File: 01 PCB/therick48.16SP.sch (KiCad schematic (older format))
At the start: 172 parts, among them J1 TYPE-C-31-M12_13, J2 AVR-ISP-6_mod, K1 KEYSW, K10 KEYSW, K11 KEYSW, K12 KEYSW, K13 KEYSW, K14 KEYSW, K15 KEYSW, K16 KEYSW, K17 KEYSW, K18 KEYSW, K19 KEYSW, K2 KEYSW, K20 KEYSW, K21 KEYSW, K22 KEYSW, K23 KEYSW, K24 KEYSW, K25 KEYSW, K26 KEYSW, K27 KEYSW, K28 KEYSW, K29 KEYSW, K3 KEYSW, K30 KEYSW, K31 KEYSW, K32 KEYSW, K33 KEYSW, K34 KEYSW, K35 KEYSW, K36 KEYSW, K37 KEYSW, K38 KEYSW, K39 KEYSW, K4 KEYSW, K40 KEYSW, K41 KEYSW, K42 KEYSW, K43 KEYSW, K44 KEYSW, K45 KEYSW, K46 KEYSW, K47 KEYSW, K48 KEYSW, K49 KEYSW, K5 KEYSW, K50 KEYSW, K51 KEYSW, K52 KEYSW, K53 KEYSW, K54 KEYSW, K55 KEYSW, K56 KEYSW, K57 KEYSW, K58 KEYSW, K59 KEYSW, K6 KEYSW, K60 KEYSW, K61 KEYSW, K62 KEYSW, K63 KEYSW, K64 KEYSW, K7 KEYSW, K8 KEYSW, K9 KEYSW, SW1 SW_PUSH, U1 ATMEGA32U4, U2 HOLE, U3 USBLC6-2SC6, U4 HOLE, U5 HOLE, U6 HOLE, U7 HOLE, Y1 16MHz

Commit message: Change 48+16SP to 48.16SP
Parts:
- added U8: HOLE, Artwork:THERICK, symbol lets_split-cache:HOLE
- H1, H10, H11, H12, H13, H14, H15, H16, H17, H18, H2, H3, H4, H5, H6, H7, H8, H9: footprint random-keyboard-parts:plate_hole_4mm_tht -> random-keyboard-parts:Generic-Mounthole
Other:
- note added: ".16 Holes"
- note added: "Planck Holes"
- note added: "THERICK"
- note added: "therick Screw Holes"
- note removed: "Screw Holes"
- moved on the sheet: H10, H11, H12, H13, H14, H15, H16, H17, H18, H4, H5, H6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

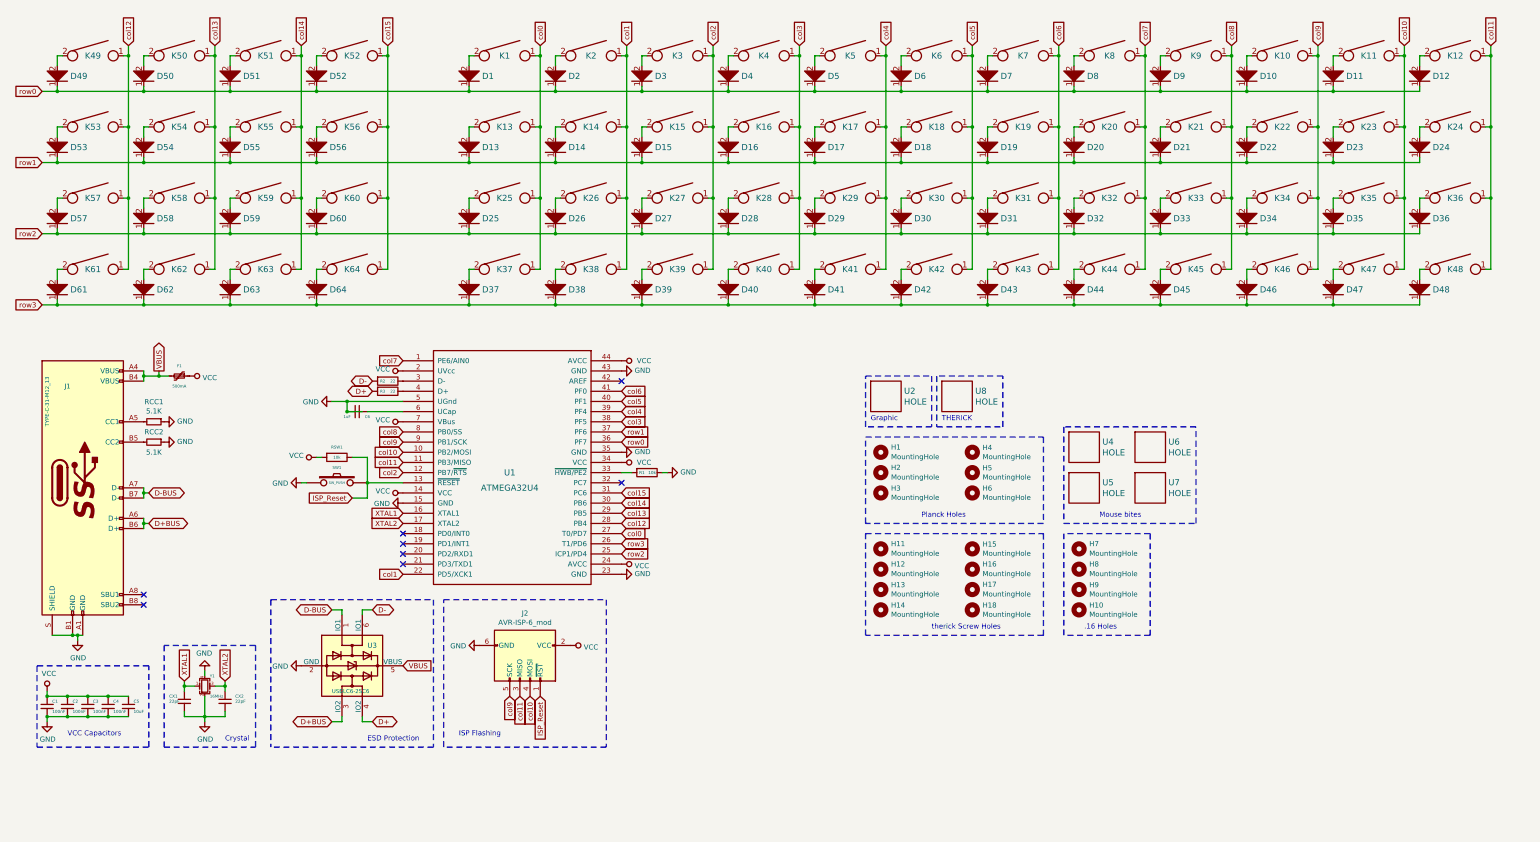
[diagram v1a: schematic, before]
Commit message: Add power LED
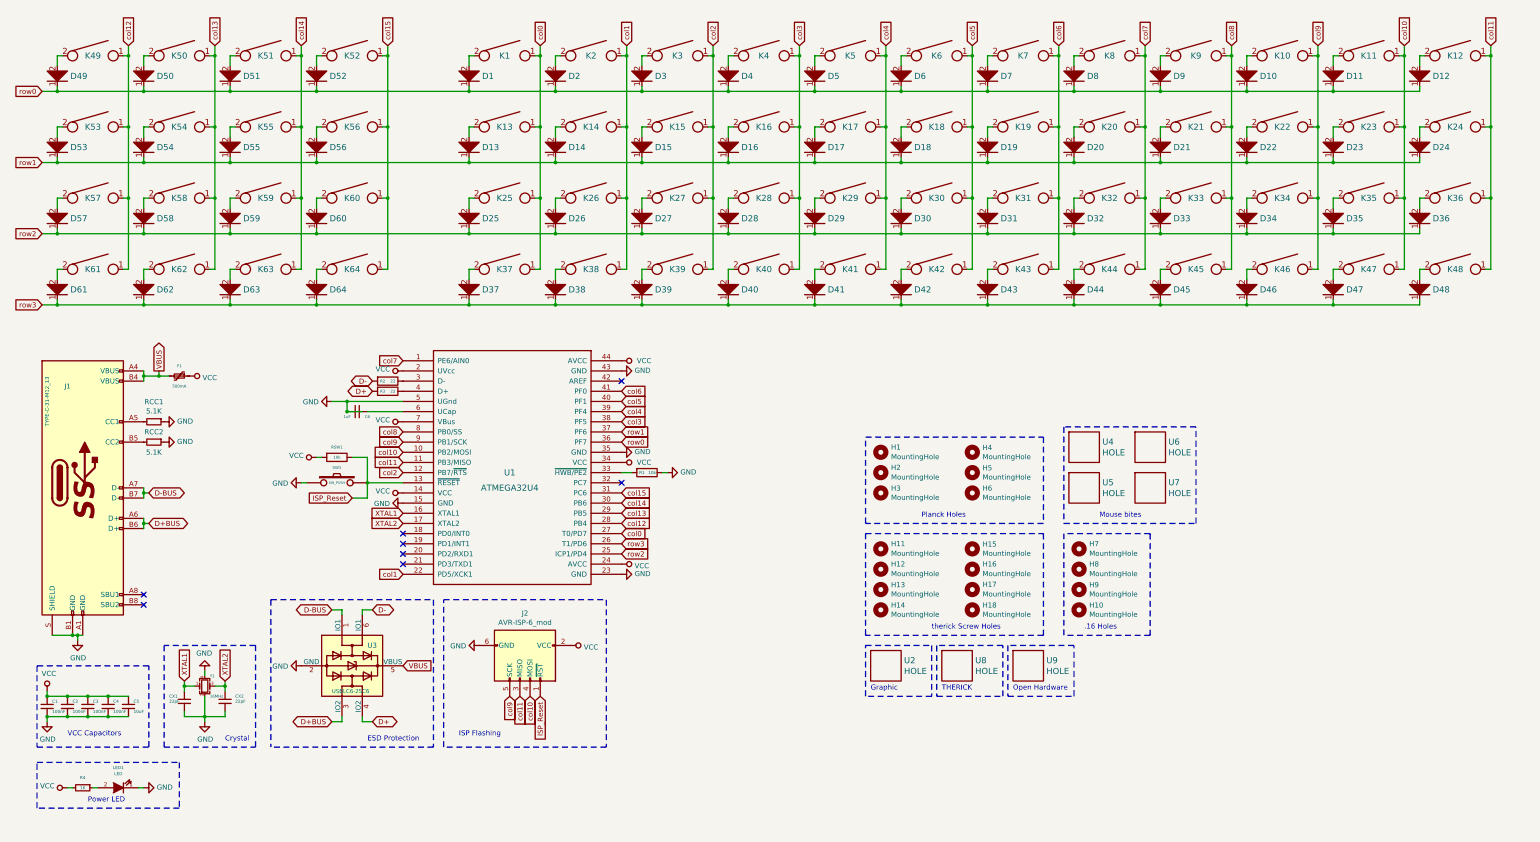
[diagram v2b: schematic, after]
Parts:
- added LED1: LED, LED_SMD:LED_0805_2012Metric_Pad1.15x1.40mm_HandSolder, symbol keyboard_parts:LED
- added R4: 1K, Resistor_SMD:R_0805_2012Metric_Pad1.15x1.40mm_HandSolder, symbol Device:R_Small
- added U9: HOLE, Symbol:OSHW-Logo2_9.8x8mm_SilkScreen, symbol lets_split-cache:HOLE
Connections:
- net GND: now also LED1.1 (K)
- net VCC: now also R4.2
- new net: LED1.2 (A), R4.1
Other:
- note added: "Open Hardware"
- note added: "Power LED"
- moved on the sheet: U2, U8
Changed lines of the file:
@@
 L lets_split-cache:HOLE U2
 U 1 1 5DE56E92
-P 9300 4500
-F 0 "U2" H 9478 4553 60  0000 L CNN
-F 1 "HOLE" H 9478 4447 60  0000 L CNN
-F 2 "Artwork:rick_large" H 9300 4500 60  0001 C CNN
-F 3 "" H 9300 4500 60  0001 C CNN
-	1    9300 4500
+P 9300 7150
+F 0 "U2" H 9478 7203 60  0000 L CNN
+F 1 "HOLE" H 9478 7097 60  0000 L CNN
+F 2 "Artwork:rick_large" H 9300 7150 60  0001 C CNN
+F 3 "" H 9300 7150 60  0001 C CNN
+	1    9300 7150
 	1    0    0    -1
 $EndComp
@@
 Text Notes 9650 5700 0    50   ~ 0
 Planck Holes
-Text Notes 9150 4750 0    50   ~ 0
+Text Notes 9150 7400 0    50   ~ 0
 Graphic
 Wire Notes Line
-	9100 4800 9100 4300
+	9100 7450 9100 6950
 Wire Notes Line
-	9100 4300 9750 4300
+	9100 6950 9750 6950
 Wire Notes Line
-	9750 4300 9750 4800
+	9750 6950 9750 7450
 Wire Notes Line
-	9750 4800 9100 4800
+	9750 7450 9100 7450
 Text GLabel 2050 5750 2    50   BiDi ~ 0
 D+BUS
@@
 L lets_split-cache:HOLE U8
 U 1 1 5ED5F324
-P 10000 4500
-F 0 "U8" H 10178 4553 60  0000 L CNN
-F 1 "HOLE" H 10178 4447 60  0000 L CNN
-F 2 "Artwork:THERICK" H 10000 4500 60  0001 C CNN
-F 3 "" H 10000 4500 60  0001 C CNN
-	1    10000 4500
+P 10000 7150
+F 0 "U8" H 10178 7203 60  0000 L CNN
+F 1 "HOLE" H 10178 7097 60  0000 L CNN
+F 2 "Artwork:THERICK" H 10000 7150 60  0001 C CNN
+F 3 "" H 10000 7150 60  0001 C CNN
+	1    10000 7150
 	1    0    0    -1
 $EndComp
-Text Notes 9850 4750 0    50   ~ 0
+Text Notes 9850 7400 0    50   ~ 0
 THERICK
 Wire Notes Line
-	9800 4300 9800 4800
+	9800 6950 9800 7450
 Wire Notes Line
-	9800 4800 10450 4800
+	9800 7450 10450 7450
 Wire Notes Line
-	10450 4800 10450 4300
+	10450 7450 10450 6950
 Wire Notes Line
-	10450 4300 9800 4300
+	10450 6950 9800 6950
 Text Notes 9750 6800 0    50   ~ 0
 therick Screw Holes
@@
 Wire Notes Line
 	11050 6850 11050 5850
+$Comp
+L power:VCC #PWR0126
+U 1 1 5F9DB716
+P 1250 8350
+F 0 "#PWR0126" H 1250 8200 50  0001 C CNN
+F 1 "VCC" V 1268 8477 50  0000 L CNN
+F 2 "" H 1250 8350 50  0001 C CNN
+F 3 "" H 1250 8350 50  0001 C CNN
+	1    1250 8350
+	0    -1   -1   0
+$EndComp
+$Comp
+L Device:R_Small R4
+U 1 1 5F9DC91D
+P 1400 8350
+F 0 "R4" V 1300 8350 30  0000 C CNN
+F 1 "1K" V 1400 8350 30  0000 C CNN
+F 2 "Resistor_SMD:R_0805_2012Metric_Pad1.15x1.40mm_HandSolder" H 1400 8350 50  0001 C CNN
+F 3 "~" H 1400 8350 50  0001 C CNN
+	1    1400 8350
+	0    1    1    0
+$EndComp
+$Comp
+L keyboard_parts:LED LED1
+U 1 1 5F9DDB15
+P 1750 8350
+F 0 "LED1" H 1750 8152 30  0000 C CNN
+F 1 "LED" H 1750 8212 30  0000 C CNN
+F 2 "LED_SMD:LED_0805_2012Metric_Pad1.15x1.40mm_HandSolder" H 1750 8350 60  0001 C CNN
+F 3 "" H 1750 8350 60  0000 C CNN
+	1    1750 8350
+	-1   0    0    1
+$EndComp
+$Comp
+L power:GND #PWR0127
+U 1 1 5F9E038F
+P 2000 8350
+F 0 "#PWR0127" H 2000 8100 50  0001 C CNN
+F 1 "GND" V 2005 8222 50  0000 R CNN
+F 2 "" H 2000 8350 50  0001 C CNN
+F 3 "" H 2000 8350 50  0001 C CNN
+	1    2000 8350
+	0    -1   -1   0
+$EndComp
+Wire Wire Line
+	1250 8350 1300 8350
+Wire Wire Line
+	1500 8350 1550 8350
+Wire Wire Line
+	1950 8350 2000 8350
+Text Notes 1450 8500 0    50   ~ 0
+Power LED
+Wire Notes Line
+	950  8100 2350 8100
+Wire Notes Line
+	2350 8100 2350 8550
+Wire Notes Line
+	2350 8550 950  8550
+Wire Notes Line
+	950  8550 950  8100
+$Comp
+L lets_split-cache:HOLE U9
+U 1 1 5FDBE9BF
+P 10700 7150
+F 0 "U9" H 10878 7203 60  0000 L CNN
+F 1 "HOLE" H 10878 7097 60  0000 L CNN
+F 2 "Symbol:OSHW-Logo2_9.8x8mm_SilkScreen" H 10700 7150 60  0001 C CNN
+F 3 "" H 10700 7150 60  0001 C CNN
+	1    10700 7150
+	1    0    0    -1
+$EndComp
+Text Notes 10550 7400 0    50   ~ 0
+Open Hardware
+Wire Notes Line
+	10500 6950 10500 7450
+Wire Notes Line
+	10500 7450 11150 7450
+Wire Notes Line
+	11150 7450 11150 6950
+Wire Notes Line
+	11150 6950 10500 6950
 $EndSCHEMATC

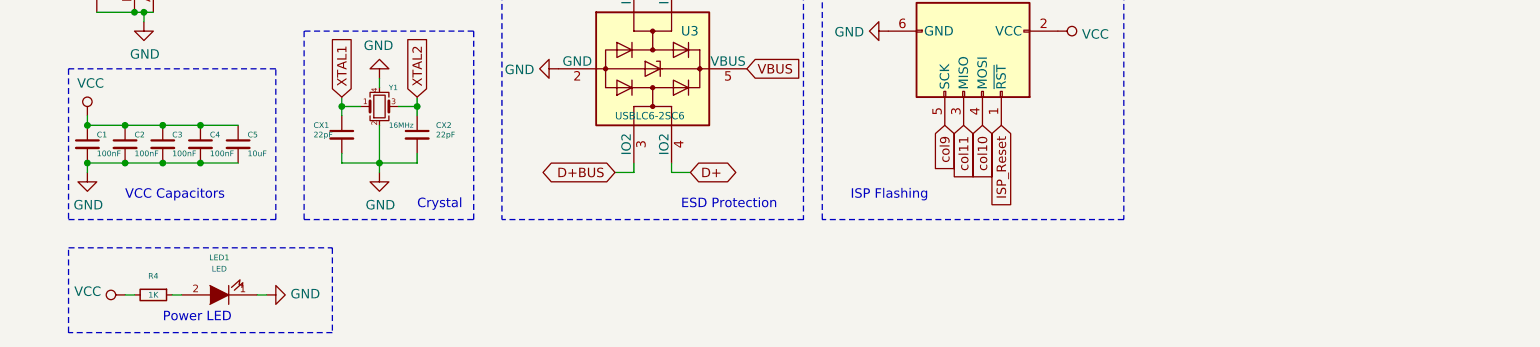
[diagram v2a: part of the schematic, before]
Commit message: Made 2 columns able to be broken away
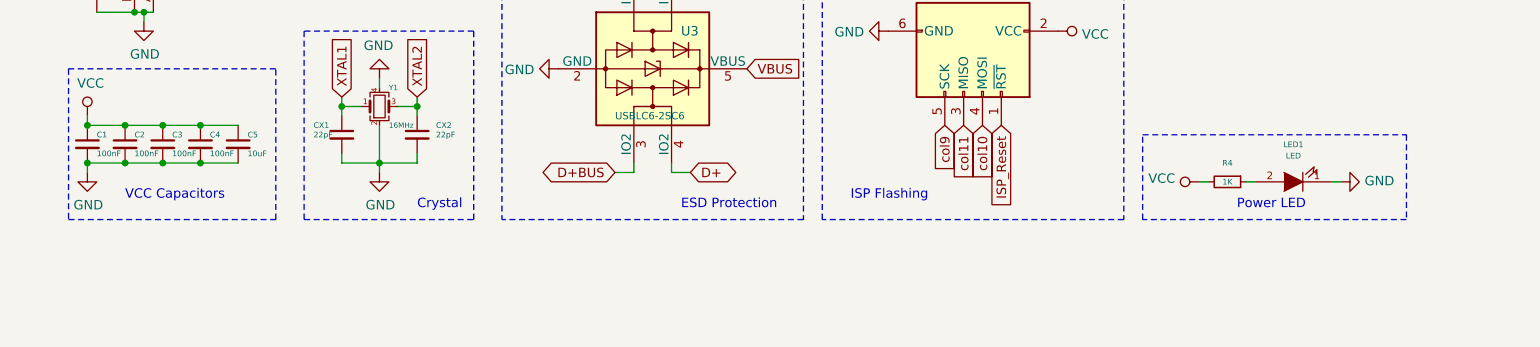
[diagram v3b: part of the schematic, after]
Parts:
- U9: footprint Symbol:OSHW-Logo2_9.8x8mm_SilkScreen -> Symbol:OSHW-Logo2_14.6x12mm_SilkScreen
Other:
- moved on the sheet: LED1, R4
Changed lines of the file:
@@
 L power:VCC #PWR0126
 U 1 1 5F9DB716
-P 1250 8350
-F 0 "#PWR0126" H 1250 8200 50  0001 C CNN
-F 1 "VCC" V 1268 8477 50  0000 L CNN
-F 2 "" H 1250 8350 50  0001 C CNN
-F 3 "" H 1250 8350 50  0001 C CNN
-	1    1250 8350
+P 6950 7750
+F 0 "#PWR0126" H 6950 7600 50  0001 C CNN
+F 1 "VCC" V 6968 7877 50  0000 L CNN
+F 2 "" H 6950 7750 50  0001 C CNN
+F 3 "" H 6950 7750 50  0001 C CNN
+	1    6950 7750
 	0    -1   -1   0
 $EndComp
@@
 L Device:R_Small R4
 U 1 1 5F9DC91D
-P 1400 8350
-F 0 "R4" V 1300 8350 30  0000 C CNN
-F 1 "1K" V 1400 8350 30  0000 C CNN
-F 2 "Resistor_SMD:R_0805_2012Metric_Pad1.15x1.40mm_HandSolder" H 1400 8350 50  0001 C CNN
-F 3 "~" H 1400 8350 50  0001 C CNN
-	1    1400 8350
+P 7100 7750
+F 0 "R4" V 7000 7750 30  0000 C CNN
+F 1 "1K" V 7100 7750 30  0000 C CNN
+F 2 "Resistor_SMD:R_0805_2012Metric_Pad1.15x1.40mm_HandSolder" H 7100 7750 50  0001 C CNN
+F 3 "~" H 7100 7750 50  0001 C CNN
+	1    7100 7750
 	0    1    1    0
 $EndComp
@@
 L keyboard_parts:LED LED1
 U 1 1 5F9DDB15
-P 1750 8350
-F 0 "LED1" H 1750 8152 30  0000 C CNN
-F 1 "LED" H 1750 8212 30  0000 C CNN
-F 2 "LED_SMD:LED_0805_2012Metric_Pad1.15x1.40mm_HandSolder" H 1750 8350 60  0001 C CNN
-F 3 "" H 1750 8350 60  0000 C CNN
-	1    1750 8350
+P 7450 7750
+F 0 "LED1" H 7450 7552 30  0000 C CNN
+F 1 "LED" H 7450 7612 30  0000 C CNN
+F 2 "LED_SMD:LED_0805_2012Metric_Pad1.15x1.40mm_HandSolder" H 7450 7750 60  0001 C CNN
+F 3 "" H 7450 7750 60  0000 C CNN
+	1    7450 7750
 	-1   0    0    1
 $EndComp
@@
 L power:GND #PWR0127
 U 1 1 5F9E038F
-P 2000 8350
-F 0 "#PWR0127" H 2000 8100 50  0001 C CNN
-F 1 "GND" V 2005 8222 50  0000 R CNN
-F 2 "" H 2000 8350 50  0001 C CNN
-F 3 "" H 2000 8350 50  0001 C CNN
-	1    2000 8350
+P 7700 7750
+F 0 "#PWR0127" H 7700 7500 50  0001 C CNN
+F 1 "GND" V 7705 7622 50  0000 R CNN
+F 2 "" H 7700 7750 50  0001 C CNN
+F 3 "" H 7700 7750 50  0001 C CNN
+	1    7700 7750
 	0    -1   -1   0
 $EndComp
 Wire Wire Line
-	1250 8350 1300 8350
+	6950 7750 7000 7750
 Wire Wire Line
-	1500 8350 1550 8350
+	7200 7750 7250 7750
 Wire Wire Line
-	1950 8350 2000 8350
-Text Notes 1450 8500 0    50   ~ 0
+	7650 7750 7700 7750
+Text Notes 7150 7900 0    50   ~ 0
 Power LED
 Wire Notes Line
-	950  8100 2350 8100
+	6650 7500 8050 7500
 Wire Notes Line
-	2350 8100 2350 8550
+	8050 7500 8050 7950
 Wire Notes Line
-	2350 8550 950  8550
+	8050 7950 6650 7950
 Wire Notes Line
-	950  8550 950  8100
+	6650 7950 6650 7500
 $Comp
 L lets_split-cache:HOLE U9
@@
 F 0 "U9" H 10878 7203 60  0000 L CNN
 F 1 "HOLE" H 10878 7097 60  0000 L CNN
-F 2 "Symbol:OSHW-Logo2_9.8x8mm_SilkScreen" H 10700 7150 60  0001 C CNN
+F 2 "Symbol:OSHW-Logo2_14.6x12mm_SilkScreen" H 10700 7150 60  0001 C CNN
 F 3 "" H 10700 7150 60  0001 C CNN
 	1    10700 7150

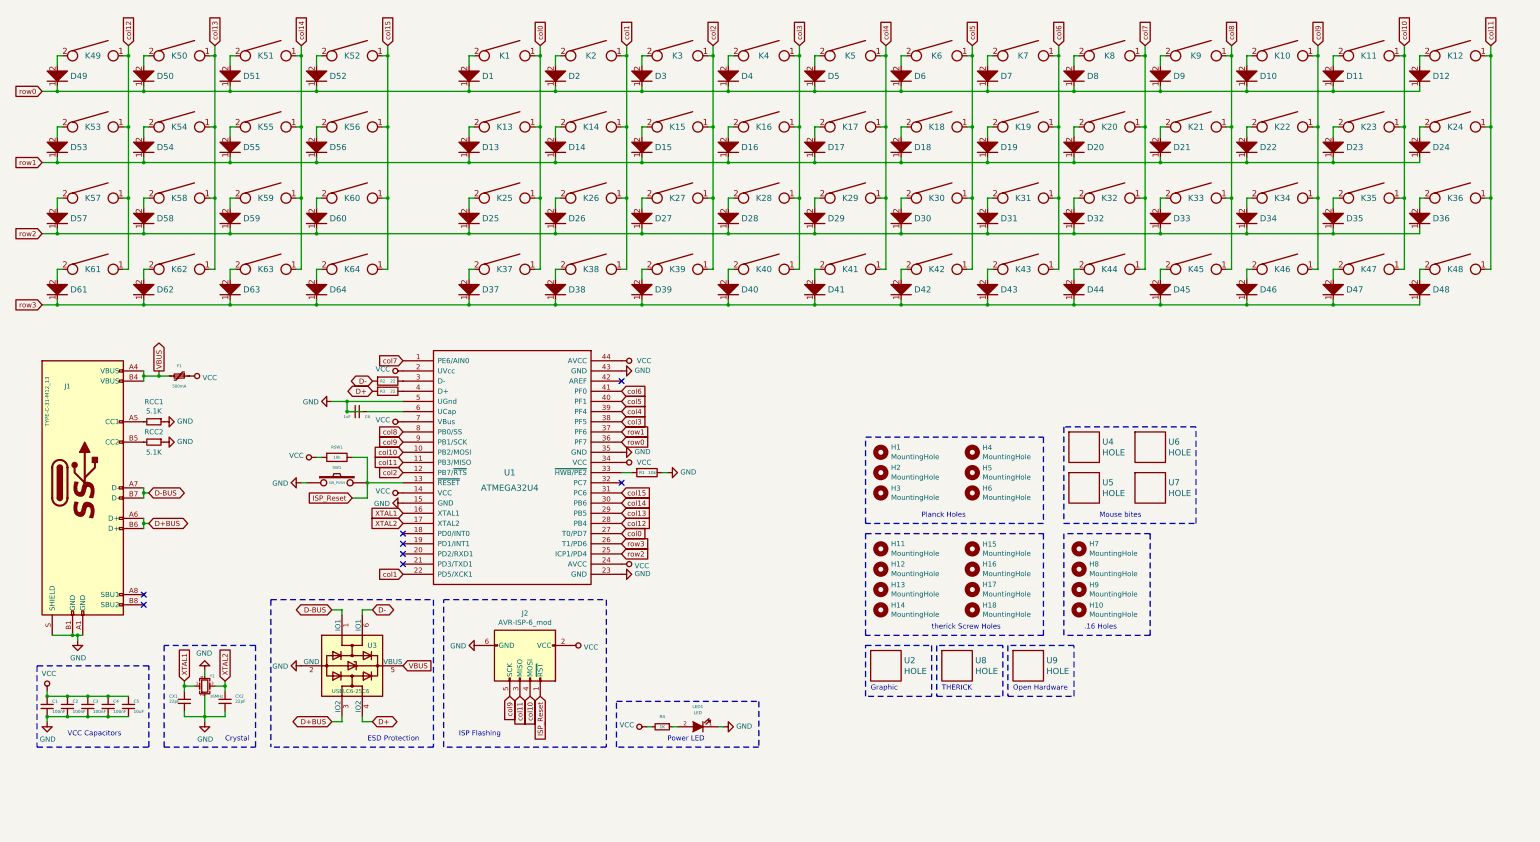
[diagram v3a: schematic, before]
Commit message: Added breakaway section, added rotary encoder support
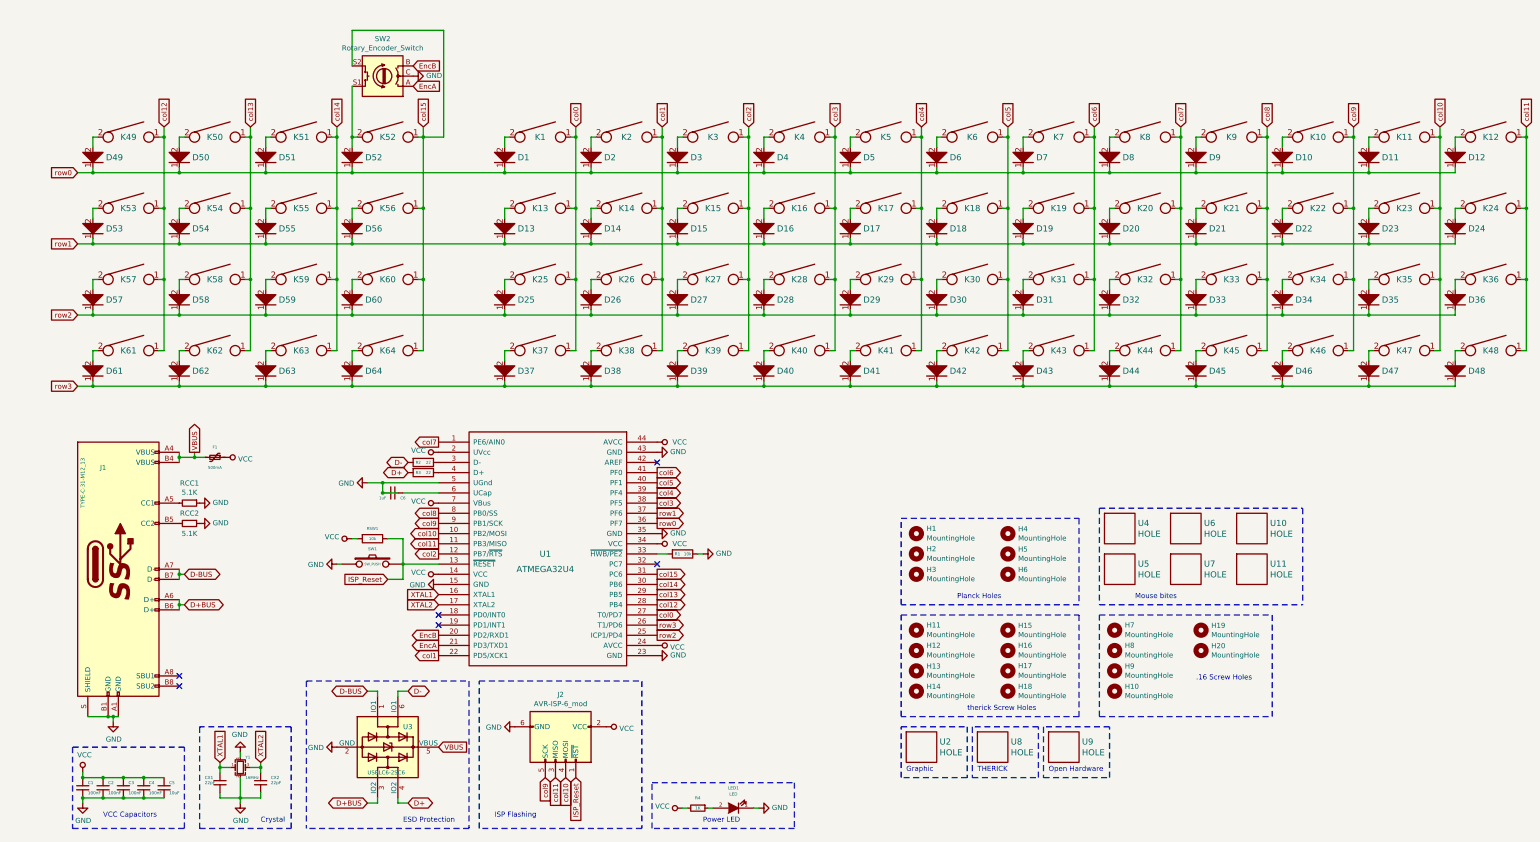
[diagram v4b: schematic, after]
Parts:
- added H19, H20: MountingHole, random-keyboard-parts:Generic-Mounthole, symbol Mechanical:MountingHole
- added SW2: Rotary_Encoder_Switch, Keebio-Parts:RotaryEncoder_EC11, symbol Device:Rotary_Encoder_Switch
- added U10, U11: HOLE, Keeb_footprints:MouseBite_IPC7351, symbol lets_split-cache:HOLE
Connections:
- net GND: now also SW2.C
- net col15: now also SW2.S2
- net EncB: now reaches U1.20 (PD2/RXD1)
- net EncB: now also SW2.B
- net EncA: now reaches U1.21 (PD3/TXD1)
- net EncA: now also SW2.A
- net at D52.2, K52.2: now also SW2.S1
- no-connect marks 8 -> 6
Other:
- note added: ".16 Screw Holes"
- note removed: ".16 Holes"
- moved on the sheet: C1, C2, C3, C4, C5, C6, CX1, CX2, D1, D10, D11, D12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
